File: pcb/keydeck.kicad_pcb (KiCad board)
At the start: 2 copper layers, 61.9 x 62.6 mm, 9 parts, among them SW1 SW_Push, SW2 SW_Push, SW3 SW_Push, SW4 SW_Push, SW5 SW_Push, U1 XIAO-RP2040-DIP

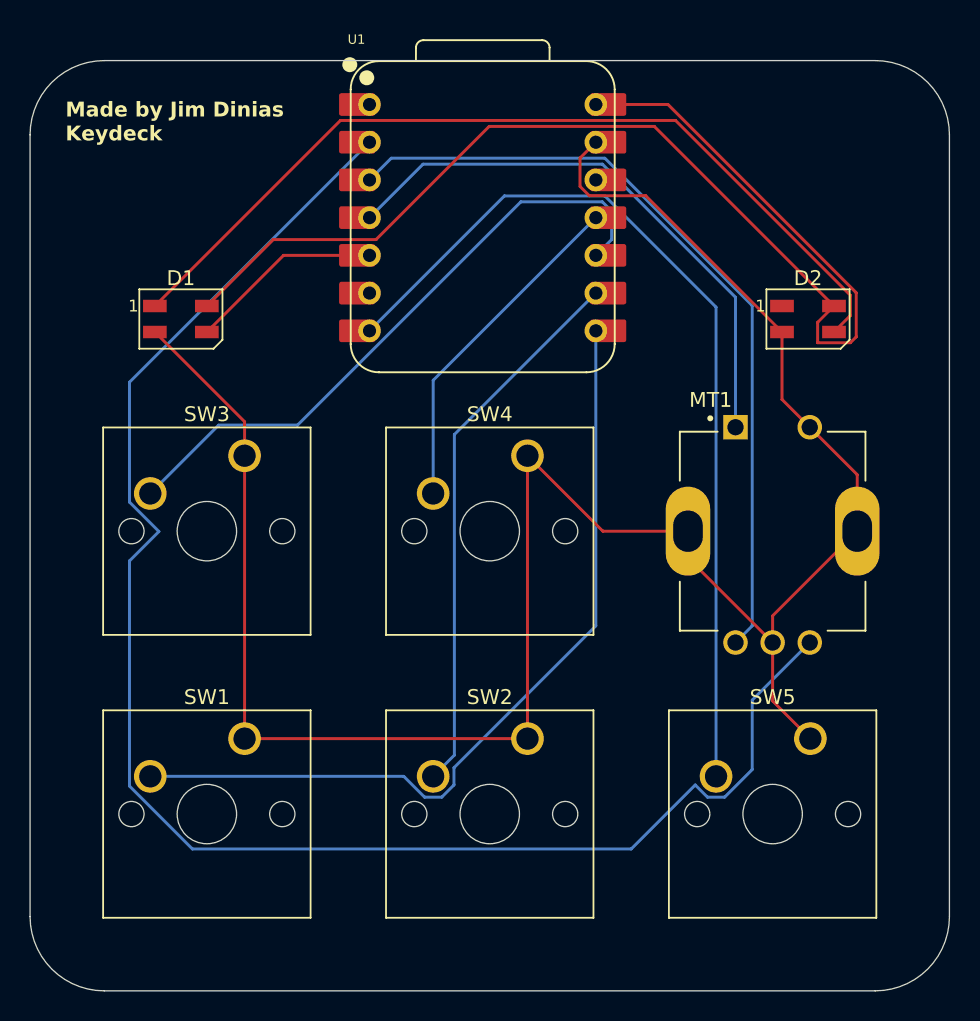
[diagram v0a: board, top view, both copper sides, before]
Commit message: round edges on pcb & fix 90 degrees routing
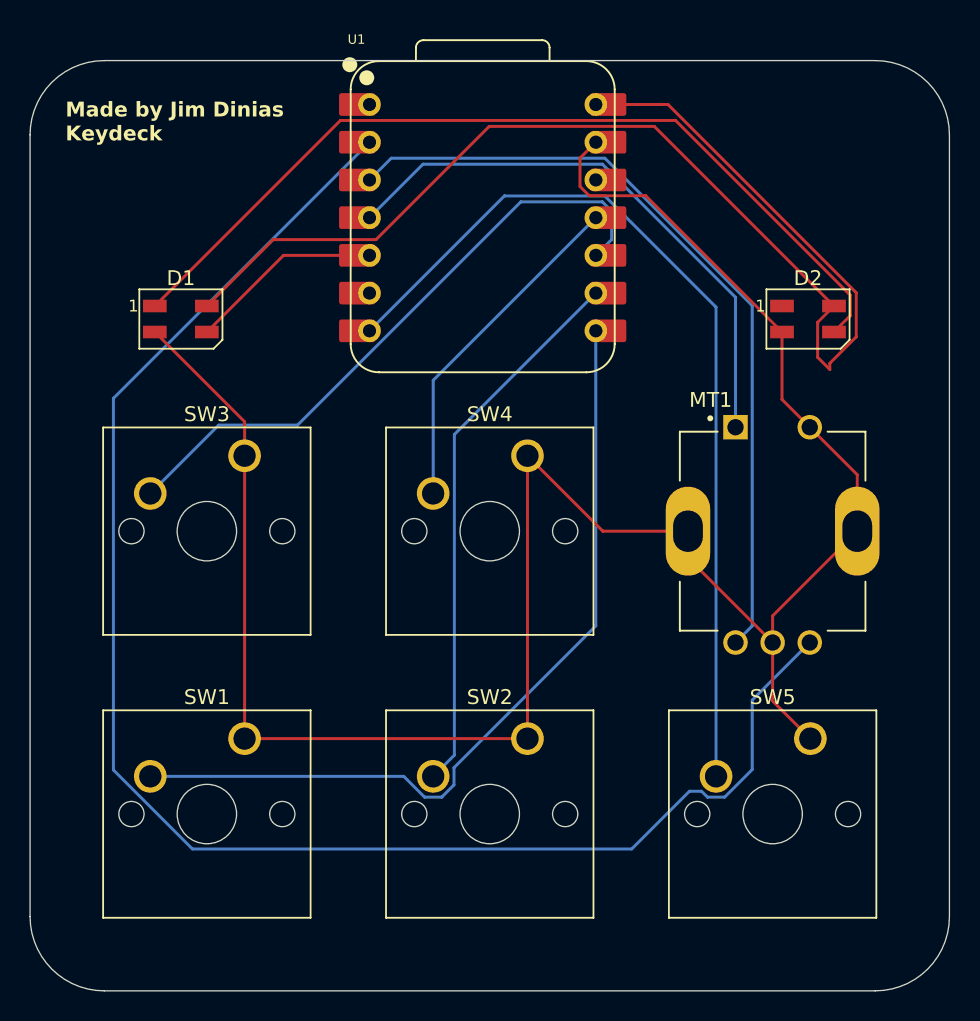
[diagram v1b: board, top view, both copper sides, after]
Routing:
- net +5V: track 83.7 -> 86.0 mm
- net Net-(U1-GPIO27/ADC1/A1): track 108.4 -> 107.3 mm
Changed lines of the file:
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@@
 	)
 	(segment
-		(start 59.08275 80.584192)
-		(end 59.08275 95.745066)
-		(width 0.2)
-		(layer "B.Cu")
-		(net 5)
-	)
-	(segment
-		(start 75.2475 52.3875)
-		(end 59.08275 68.55225)
+		(start 101.01975 94.636564)
+		(end 99.164064 96.49225)
+		(width 0.2)
+		(layer "B.Cu")
+		(net 5)
+	)
+	(segment
+		(start 97.605593 96.094407)
+		(end 96.794407 96.094407)
+		(width 0.2)
+		(layer "B.Cu")
+		(net 5)
+	)
+	(segment
+		(start 104.89375 86.08125)
+		(end 101.01975 89.95525)
+		(width 0.2)
+		(layer "B.Cu")
+		(net 5)
+	)
+	(segment
+		(start 92.906564 99.98225)
+		(end 63.319934 99.98225)
+		(width 0.2)
+		(layer "B.Cu")
+		(net 5)
+	)
+	(segment
+		(start 58 69.635)
+		(end 75.2475 52.3875)
+		(width 0.2)
+		(layer "B.Cu")
+		(net 5)
+	)
+	(segment
+		(start 96.794407 96.094407)
+		(end 92.906564 99.98225)
+		(width 0.2)
+		(layer "B.Cu")
+		(net 5)
+	)
+	(segment
+		(start 99.164064 96.49225)
+		(end 98.003436 96.49225)
+		(width 0.2)
+		(layer "B.Cu")
+		(net 5)
+	)
+	(segment
+		(start 63.319934 99.98225)
+		(end 58 94.662316)
+		(width 0.2)
+		(layer "B.Cu")
+		(net 5)
+	)
+	(segment
+		(start 101.01975 89.95525)
+		(end 101.01975 94.636564)
+		(width 0.2)
+		(layer "B.Cu")
+		(net 5)
+	)
+	(segment
+		(start 58 94.662316)
+		(end 58 69.635)
 		(width 0.2)
 		(layer "B.Cu")
@@
 	(segment
 		(start 98.003436 96.49225)
-		(end 99.164064 96.49225)
-		(width 0.2)
-		(layer "B.Cu")
-		(net 5)
-	)
-	(segment
-		(start 59.08275 76.621564)
-		(end 61.064064 78.602878)
-		(width 0.2)
-		(layer "B.Cu")
-		(net 5)
-	)
-	(segment
-		(start 101.01975 94.636564)
-		(end 101.01975 89.95525)
-		(width 0.2)
-		(layer "B.Cu")
-		(net 5)
-	)
-	(segment
-		(start 61.064064 78.602878)
-		(end 59.08275 80.584192)
-		(width 0.2)
-		(layer "B.Cu")
-		(net 5)
-	)
-	(segment
-		(start 97.18275 95.671564)
-		(end 98.003436 96.49225)
-		(width 0.2)
-		(layer "B.Cu")
-		(net 5)
-	)
-	(segment
-		(start 99.164064 96.49225)
-		(end 101.01975 94.636564)
-		(width 0.2)
-		(layer "B.Cu")
-		(net 5)
-	)
-	(segment
-		(start 63.319934 99.98225)
-		(end 92.872064 99.98225)
-		(width 0.2)
-		(layer "B.Cu")
-		(net 5)
-	)
-	(segment
-		(start 101.01975 89.95525)
-		(end 104.89375 86.08125)
-		(width 0.2)
-		(layer "B.Cu")
-		(net 5)
-	)
-	(segment
-		(start 59.08275 68.55225)
-		(end 59.08275 76.621564)
-		(width 0.2)
-		(layer "B.Cu")
-		(net 5)
-	)
-	(segment
-		(start 92.872064 99.98225)
-		(end 97.18275 95.671564)
-		(width 0.2)
-		(layer "B.Cu")
-		(net 5)
-	)
-	(segment
-		(start 59.08275 95.745066)
-		(end 63.319934 99.98225)
+		(end 97.605593 96.094407)
 		(width 0.2)
 		(layer "B.Cu")
@@
 	)
 	(segment
-		(start 105.424 65.89475)
-		(end 105.424 64.51975)
+		(start 108.027 65.49375)
+		(end 108.027 62.52665)
 		(width 0.2)
 		(layer "F.Cu")
@@
 	)
 	(segment
-		(start 105.424 64.51975)
-		(end 106.525 63.41875)
-		(width 0.2)
-		(layer "F.Cu")
-		(net 14)
-	)
-	(segment
-		(start 90.4875 49.8475)
+		(start 105.424 66.876)
+		(end 106.248 67.7)
+		(width 0.2)
+		(layer "F.Cu")
+		(net 14)
+	)
+	(segment
+		(start 106.248 67.7)
+		(end 106.248 67.27275)
+		(width 0.2)
+		(layer "F.Cu")
+		(net 14)
+	)
+	(segment
+		(start 108.027 62.52665)
 		(end 95.34785 49.8475)
 		(width 0.2)
@@
 	)
 	(segment
-		(start 107.626 65.89475)
-		(end 105.424 65.89475)
-		(width 0.2)
-		(layer "F.Cu")
-		(net 14)
-	)
-	(segment
-		(start 108.027 65.49375)
-		(end 107.626 65.89475)
+		(start 95.34785 49.8475)
+		(end 90.4875 49.8475)
 		(width 0.2)
 		(layer "F.Cu")
@@
 	)
 	(segment
-		(start 108.027 62.52665)
+		(start 106.248 67.27275)
 		(end 108.027 65.49375)
 		(width 0.2)
@@
 	)
 	(segment
-		(start 95.34785 49.8475)
-		(end 108.027 62.52665)
+		(start 105.424 64.51975)
+		(end 105.424 66.876)
 		(width 0.2)
 		(layer "F.Cu")
@@
 		(width 0.2)
 		(layer "F.Cu")
+		(net 14)
+	)
+	(segment
+		(start 106.525 63.41875)
+		(end 105.424 64.51975)
+		(width 0.2)
+		(layer "F.Cu")
